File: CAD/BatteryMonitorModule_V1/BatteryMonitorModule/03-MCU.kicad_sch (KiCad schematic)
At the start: 17 parts, among them J3 Conn_ARM_JTAG_SWD_10, J4 USB-C, SW1 BOOT0, SW2 NRST, U1 STM32G0B1CCT6, U2 INA226AQDGSRQ1

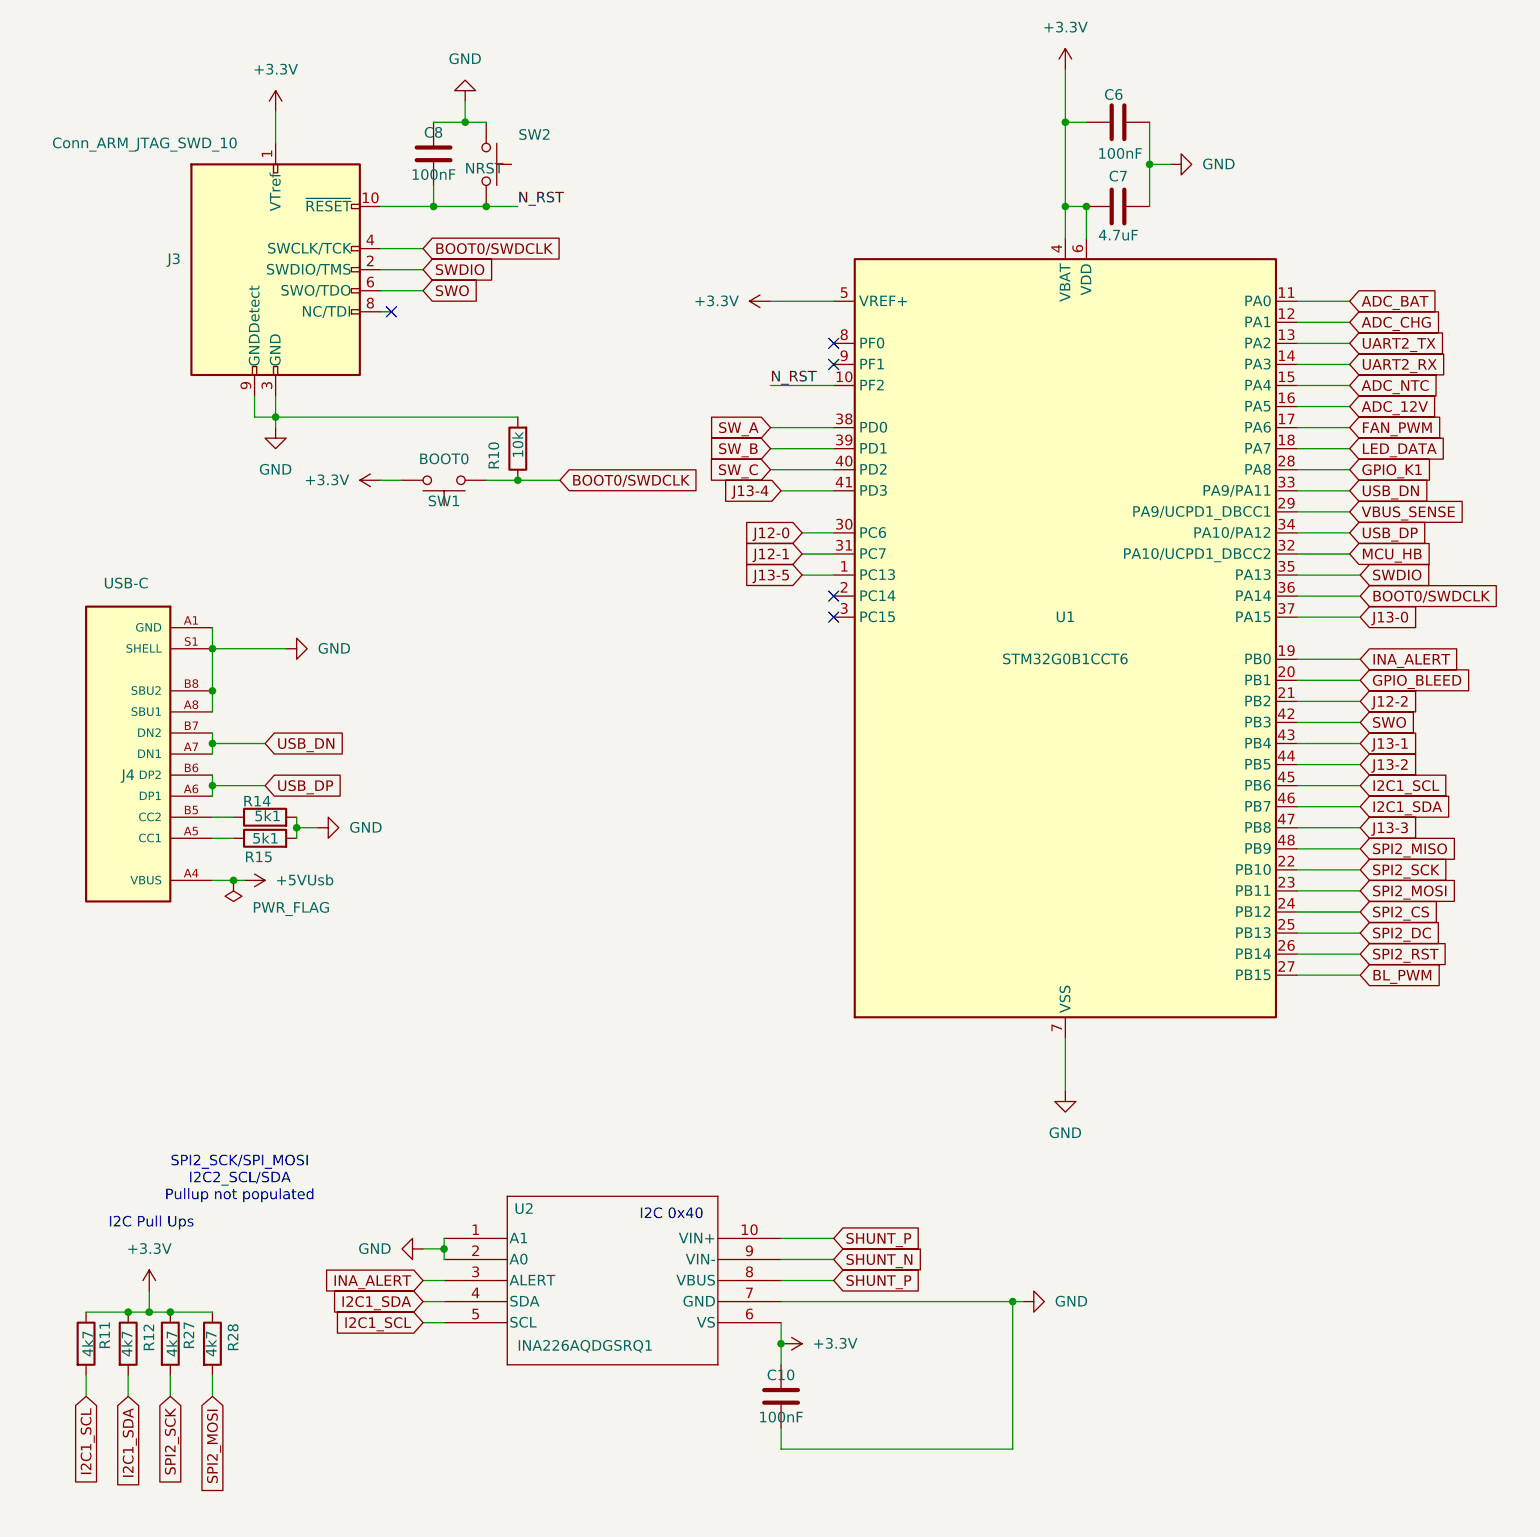
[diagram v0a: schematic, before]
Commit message: add QT06ADP83H0000G and UJ20-C USB-C connector symbols/footprints/3D models
Update V1 schematics (PowerPath, MCU, IO, top-level) to incorporate new parts.

Co-Authored-By: Claude Opus 4.7 (1M context) <noreply@anthropic.com>
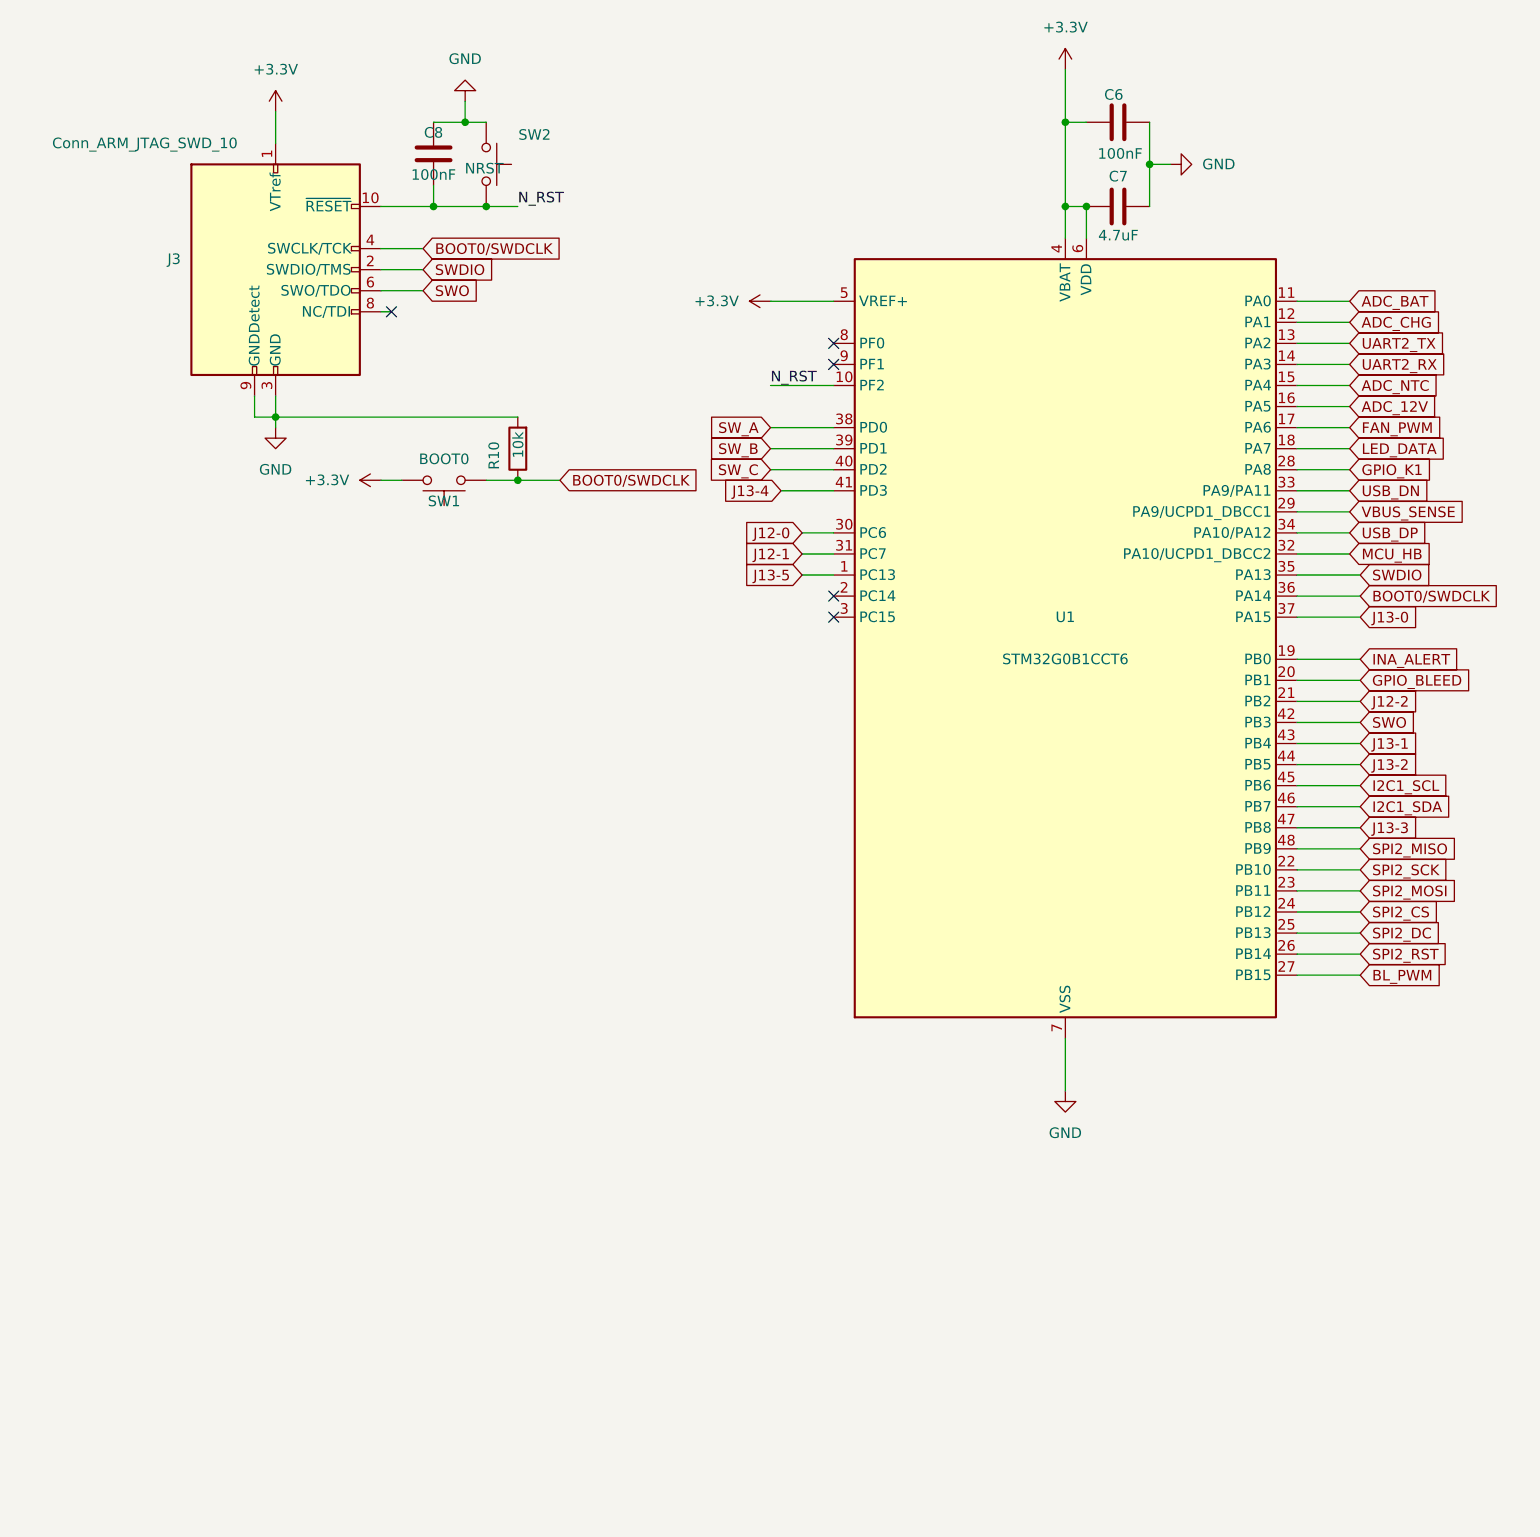
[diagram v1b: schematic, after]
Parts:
- removed C10: 100nF, Capacitor_SMD:C_0603_1608Metric, symbol Device:C
- removed J4: USB-C, BatteryMonitorModule_Custom:GCT_USB4085-GF-A_REVA4, symbol USB4085-GF-A_REVA4:USB4085-GF-A_REVA4
- removed R11, R12, R27, R28: 4k7, Resistor_SMD:R_0603_1608Metric, symbol Device:R
- removed R14, R15: 5k1, Resistor_SMD:R_0603_1608Metric, symbol Device:R
- removed U2: INA226AQDGSRQ1, Package_SO:MSOP-10_3x3mm_P0.5mm, symbol INA226AQDGSRQ1:INA226AQDGSRQ1
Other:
- note removed: "I2C 0x40"
- note removed: "I2C Pull Ups"
- note removed: "SPI2_SCK/SPI_MOSI I2C2_SCL/SDA Pullup not populated"

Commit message: add BatteryMonitorV2 STM32CubeMX project and V1 MCU schematic updates
Initial STM32CubeMX .ioc for BatteryMonitorV2. Update MCU schematic and
AP63205WU-7/INA226 custom symbols.

Co-Authored-By: Claude Opus 4.7 (1M context) <noreply@anthropic.com>
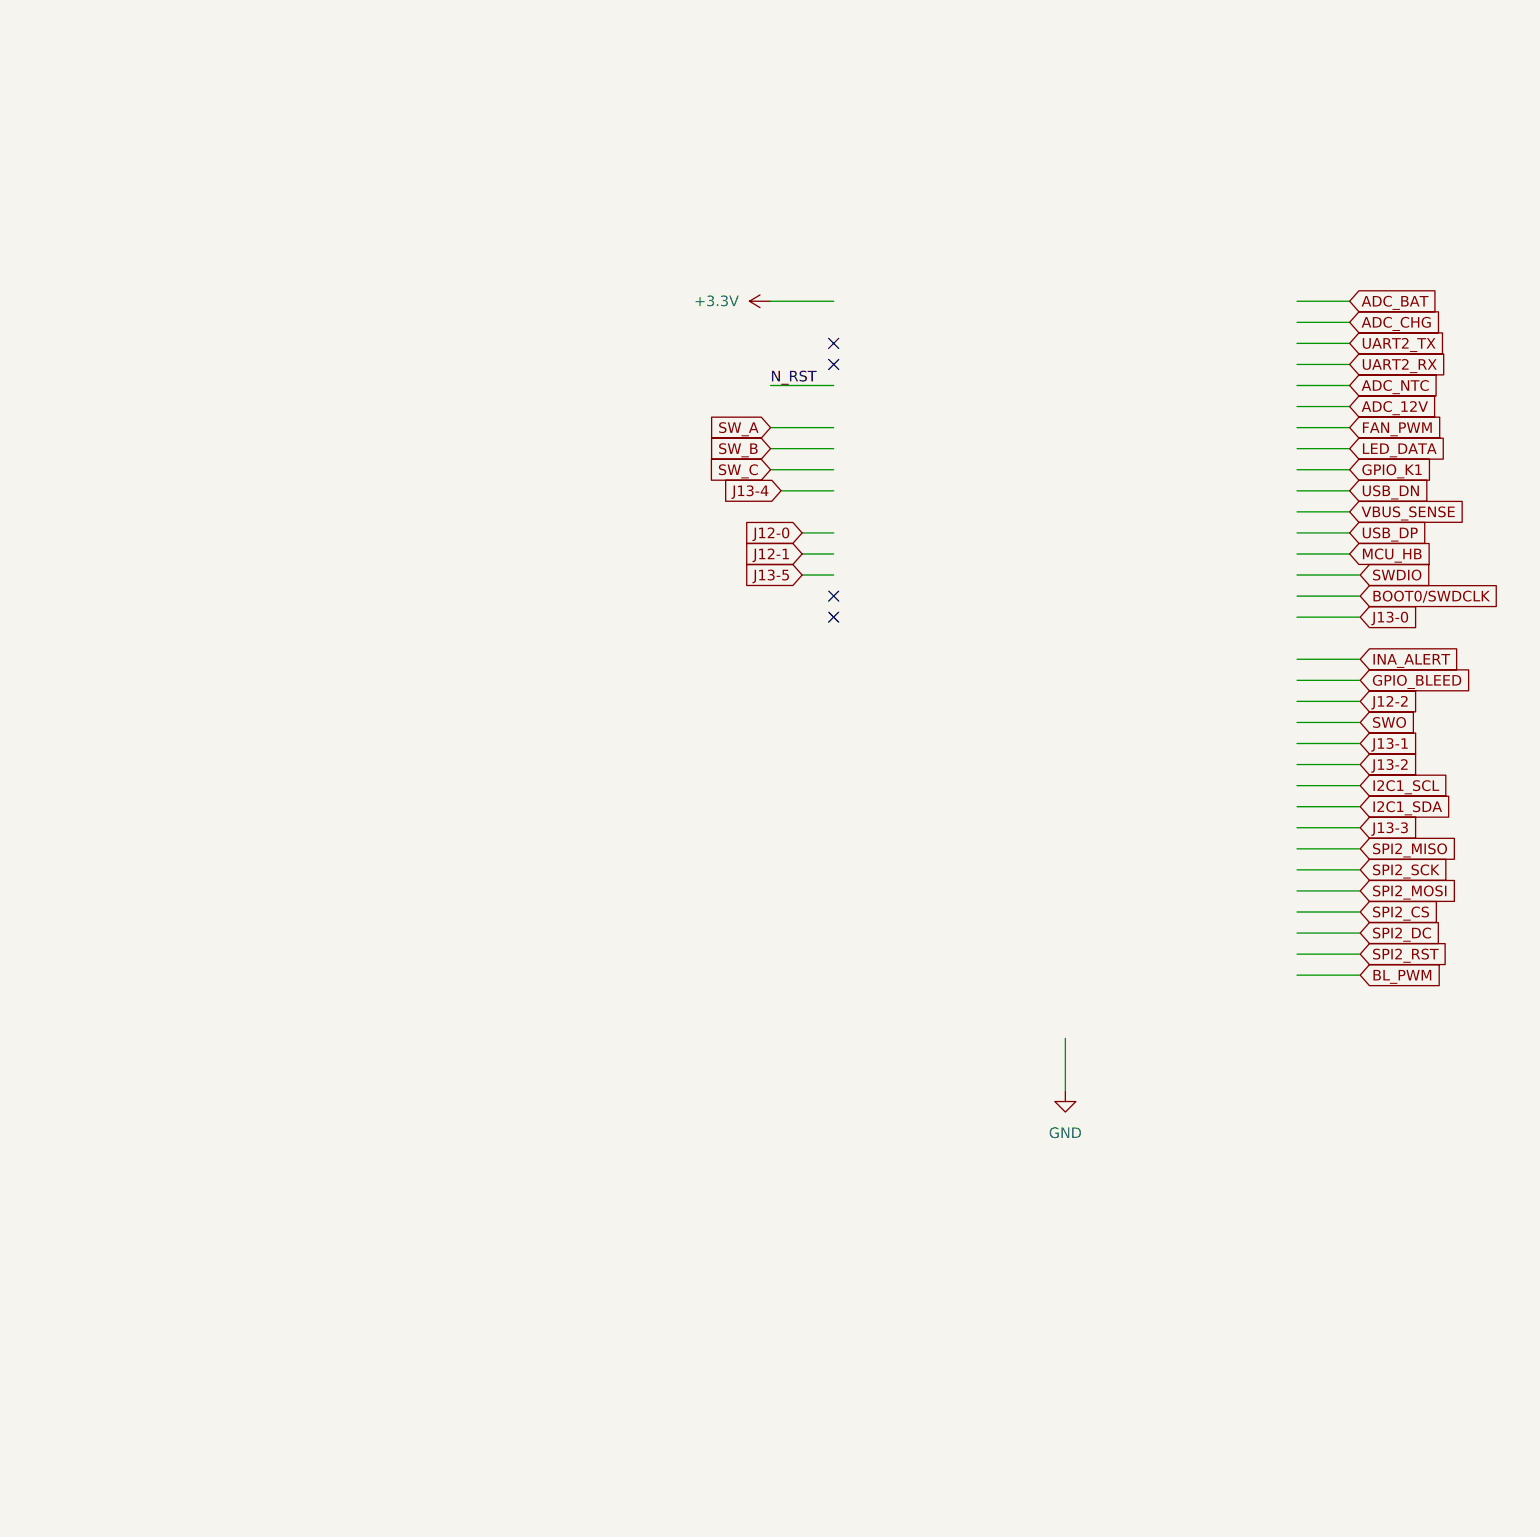
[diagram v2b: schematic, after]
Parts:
- removed C6, C8: 100nF, Capacitor_SMD:C_0603_1608Metric, symbol Device:C
- removed C7: 4.7uF, Capacitor_SMD:C_0805_2012Metric, symbol Device:C
- removed J3: Conn_ARM_JTAG_SWD_10, Connector_PinHeader_1.27mm:PinHeader_2x05_P1.27mm_Vertical_SMD, symbol Connector:Conn_ARM_JTAG_SWD_10
- removed R10: 10k, Resistor_SMD:R_0603_1608Metric, symbol Device:R
- removed SW1: BOOT0, BatteryMonitorModule_Custom:SWITCH_FSMSM_TYC, symbol Switch:SW_Push
- removed SW2: NRST, BatteryMonitorModule_Custom:SWITCH_FSMSM_TYC, symbol Switch:SW_Push
- removed U1: STM32G0B1CCT6, Package_QFP:LQFP-48_7x7mm_P0.5mm, symbol MCU_ST_STM32G0:STM32G0B1CCTx
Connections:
- no-connect marks 5 -> 4
